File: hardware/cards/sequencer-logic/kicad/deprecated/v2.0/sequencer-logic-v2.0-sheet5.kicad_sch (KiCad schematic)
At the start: 20 parts, among them IC23 74*02, IC31 74*02, IC36 74*04

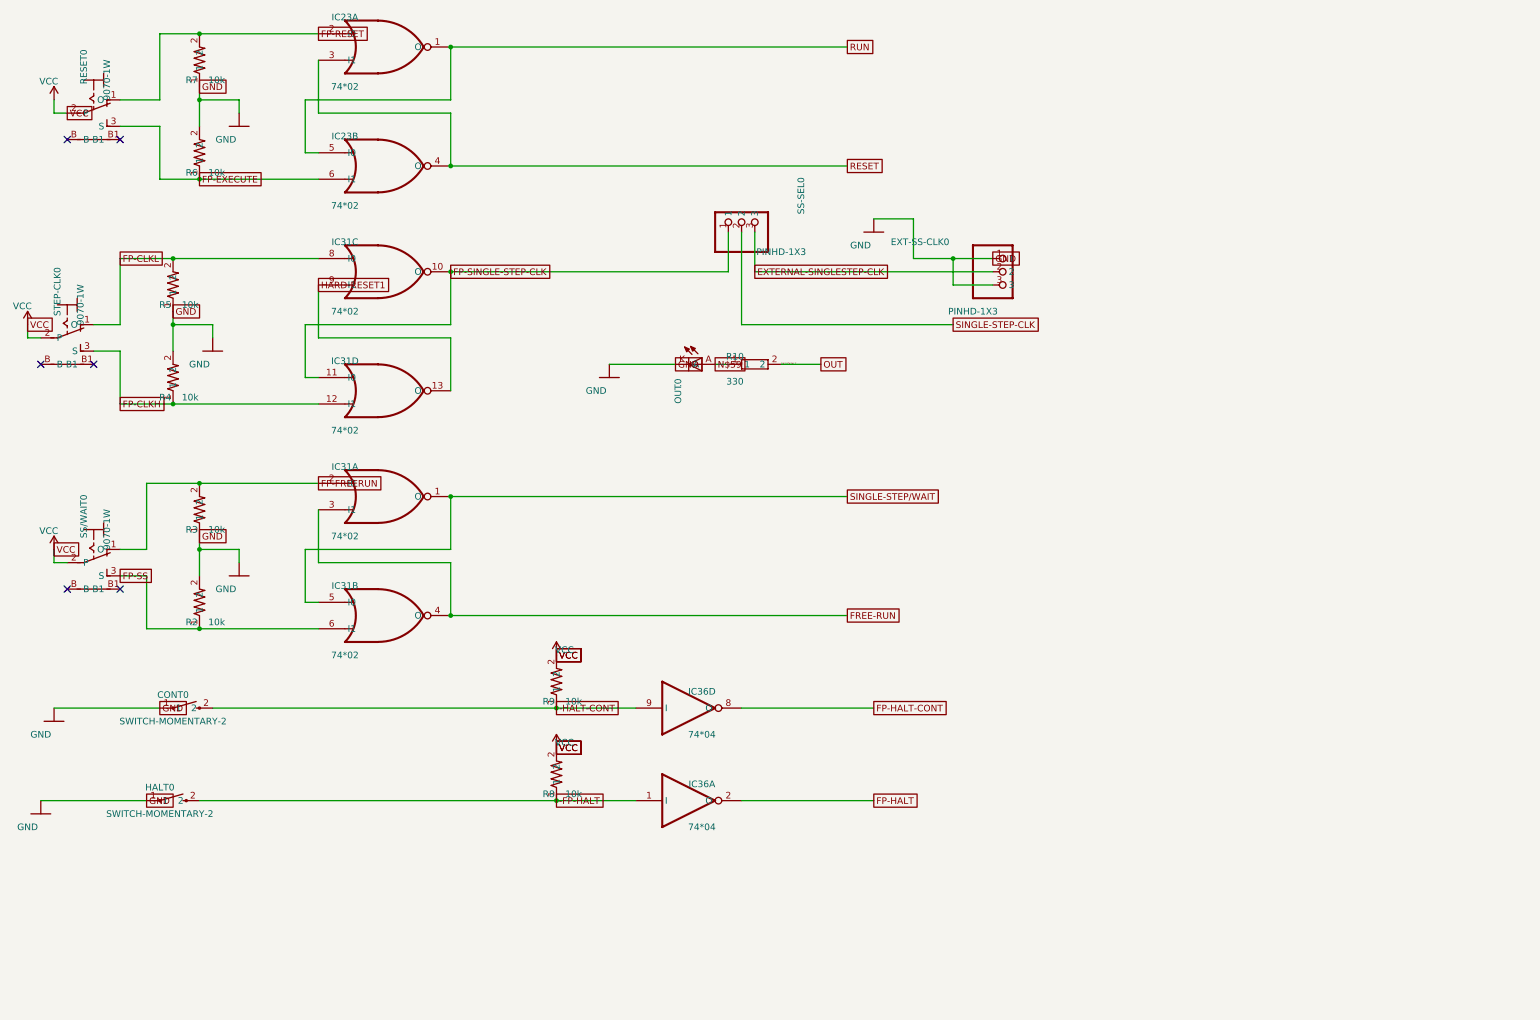
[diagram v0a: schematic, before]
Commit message: fix(kicad): readable converted schematics - overlaps 42,847 -> 3,147, nothing off the frame; CF sheet 0 overlaps
- tools/kicad/sch_overlaps.py: calibrated readability check (text/text, text/body, text/line, off frame/title block)
- eagle_sch_to_kicad.py: fields placed from Eagle's smashed attributes or the symbol's >NAME/>VALUE with Eagle's align,
  size and ratio, readable angles; fields Eagle never shows hidden (FABC96R shows only its pin name); pin numbers hidden
  where every Eagle pin hides them; Eagle-hidden layers dropped (the stray SpiceOrder text); labels on their own wires,
  converter labels only where KiCad needs them; rotate-then-mirror fixed for MR90/MR270 in pin_world/no-connects;
  each sheet on the smallest page that holds it, centred clear of the title block
- finish_board.py: stable footprint-library choice (DRC counts no longer vary run to run)
- all 37 projects regenerated: netlist proofs unchanged (34 MATCH, 2 schematic-only, video Fusion export MISMATCH as
  before); DRC same or better; ERC up (loose wire ends onto graphic buses no longer hidden by labels; explained per README)
- CF card: gate names off the gate bodies, U3 clear of its title, 5.08 mm connector pins; rebuilt: DRC 0/0, proof MATCH
- schematic PDFs regenerated (tools/sch_to_pdf.py, 37/37)

Co-Authored-By: Claude Opus 5.5 <noreply@anthropic.com>
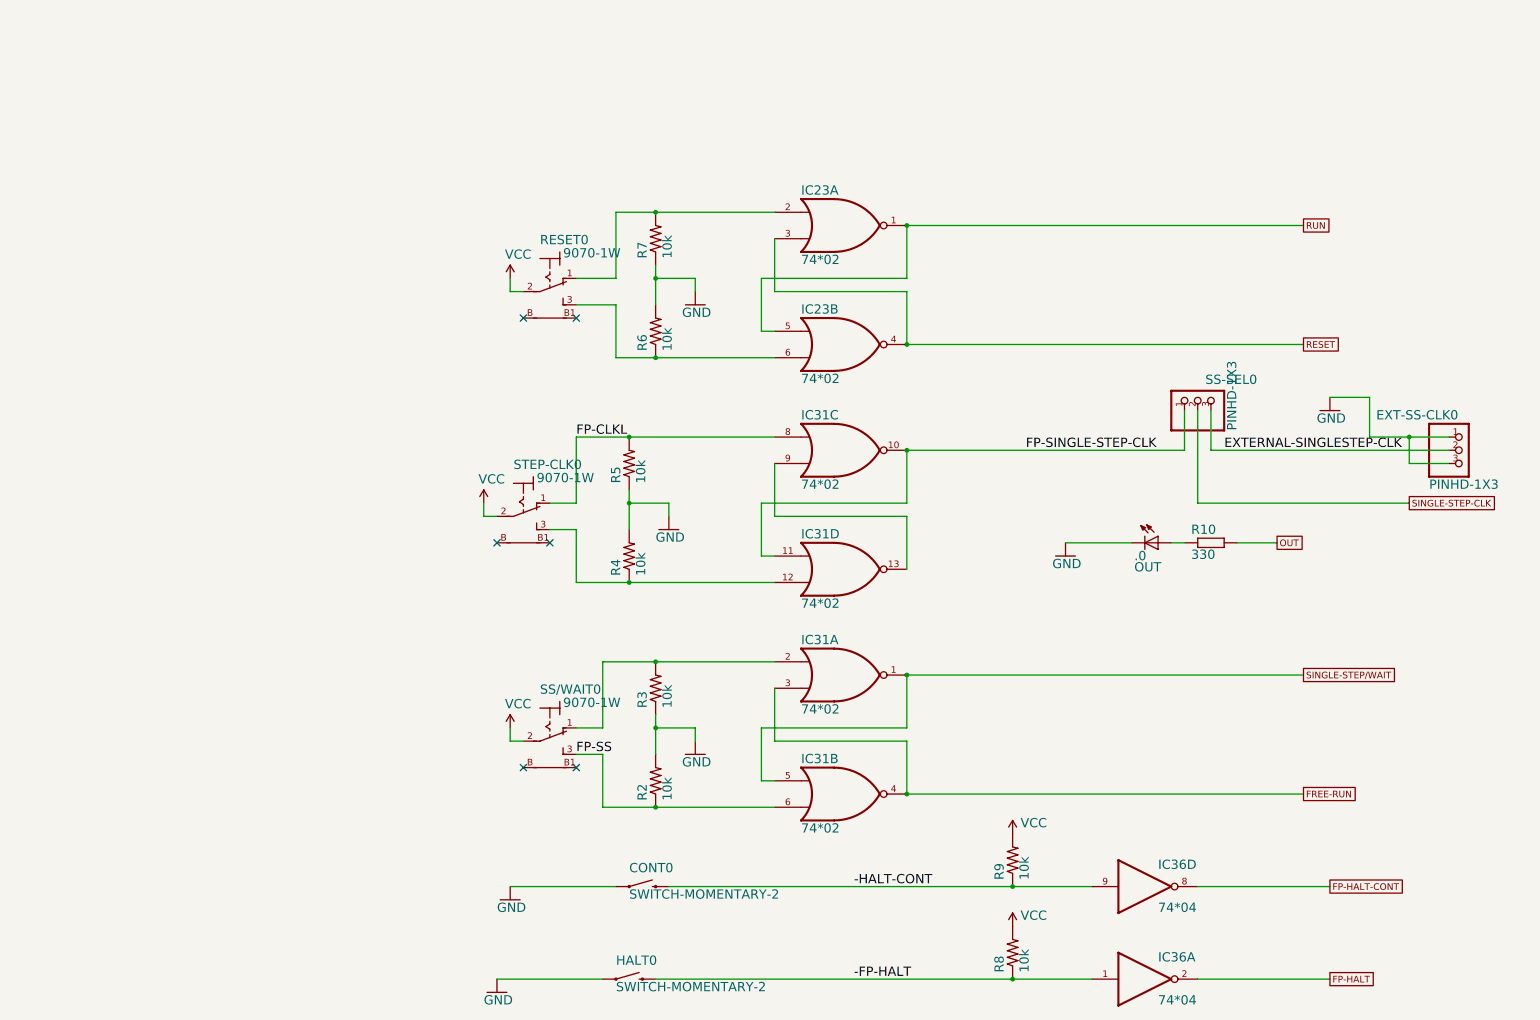
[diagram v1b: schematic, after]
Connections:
- net FP-CLKH: no longer names the net of IC31.12 (I1), R4.1, STEP-CLK0.3 (S)
- net FP-EXECUTE: no longer names the net of IC23.6 (I1), R6.1, RESET0.3 (S)
- net FP-FREERUN: no longer names the net of IC31.2 (I0), R3.2, SS/WAIT0.1 (O)
- net FP-RESET: no longer names the net of IC23.2 (I0), R7.2, RESET0.1 (O)
- net HARD-RESET1: no longer names the net of IC31.13 (O), IC31.9 (I1)
- net N$59: no longer names the net of .0.A, R10.1
